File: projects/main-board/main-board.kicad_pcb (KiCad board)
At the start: 6 copper layers, 104.8 x 77 mm, 213 parts, among them J1 TC2030, J2 TC2030, J3 S3B-PH-SM4-TB, J4 USB4105-GF-A, J5 TC2030, J6 NHD-4.3-480272EF-ASXP (Molex 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, J7 USB4105-GF-A, J8 5051101292, J9 5051101292, Q1 ZXTN4240F-7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

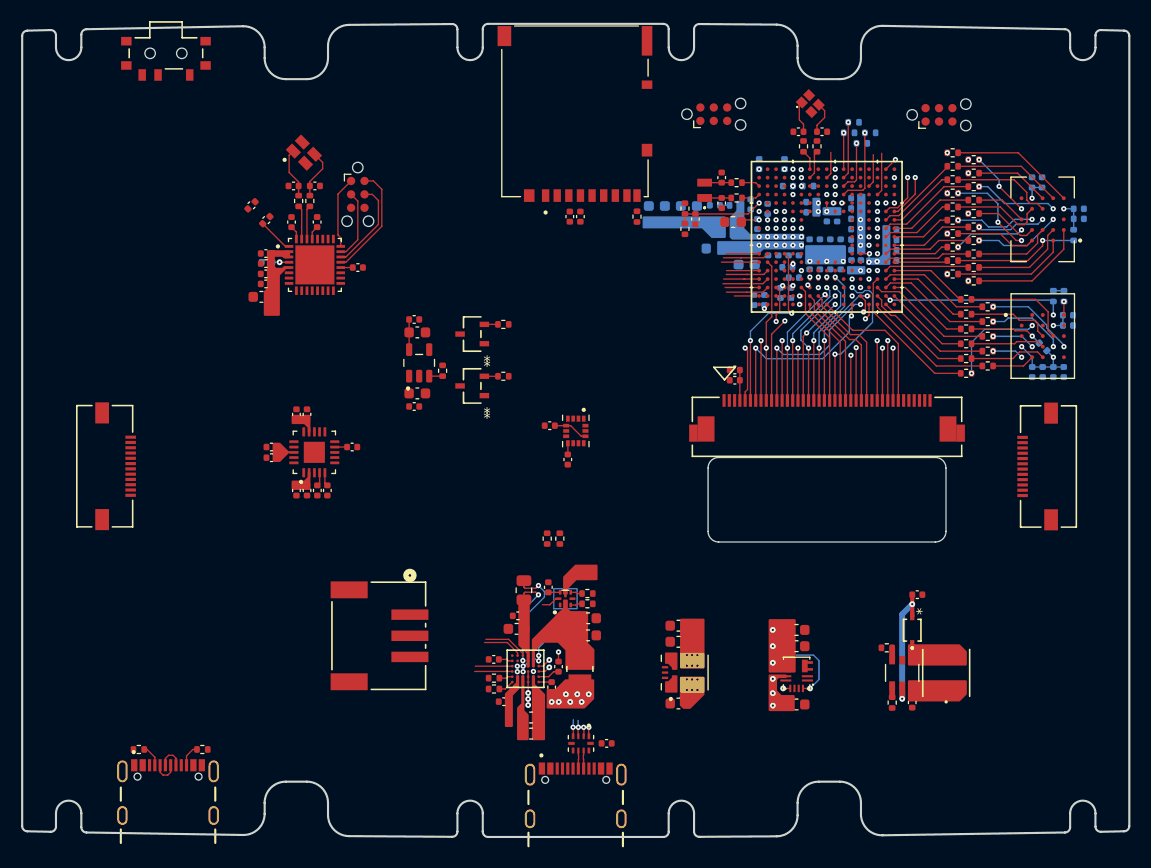
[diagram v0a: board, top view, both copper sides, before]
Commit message: Reorganise repo to support multiple PCBs
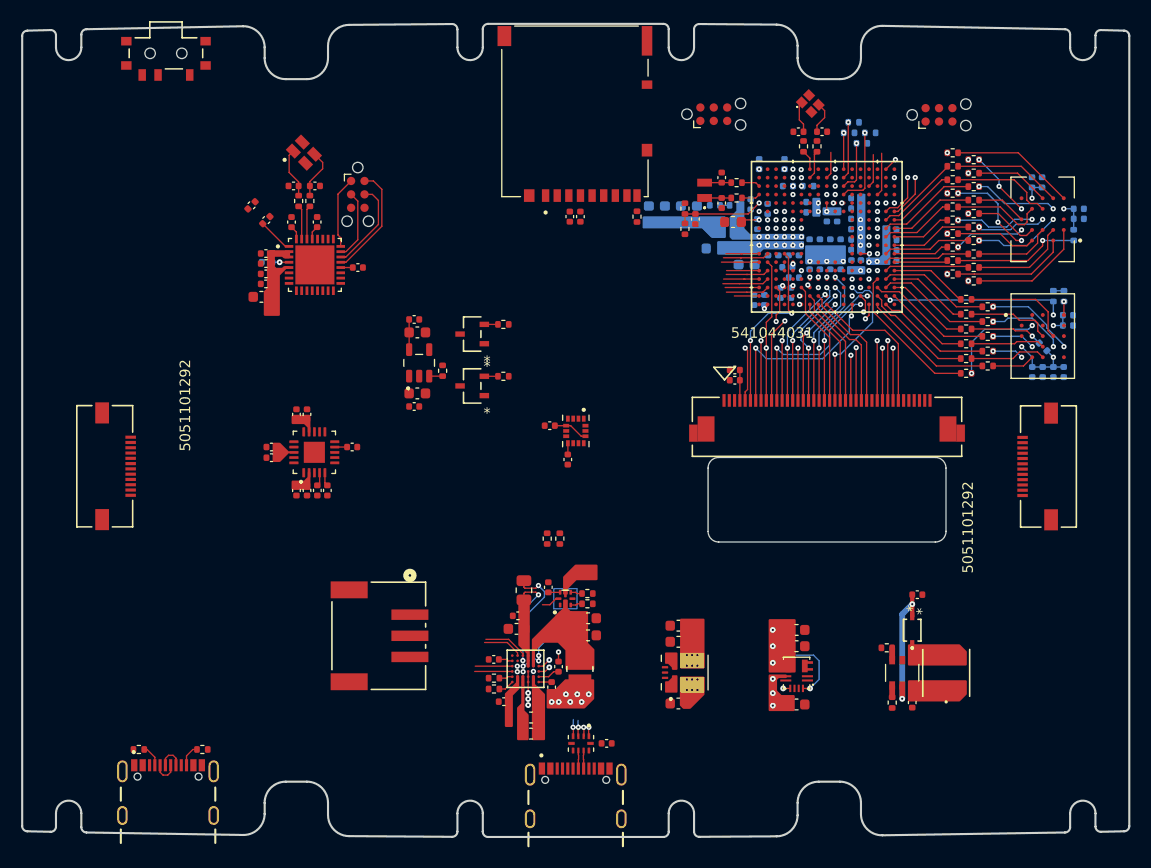
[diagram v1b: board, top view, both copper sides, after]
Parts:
- U4: value TPS22992RXPR -> TPS22992RXPR
- U7: value MAX77972EWX+T -> 21-100517_W363B3+1_ADI

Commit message: Fix wrong net name on left audio
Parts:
- U4: value TPS22992RXPR -> TPS22992RXPR
- U7: value 21-100517_W363B3+1_ADI -> MAX77972EWX+T
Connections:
- J8 pad 12: /Controllers/LEFT_MOTOR_N -> /Controllers/LEFT_MOTOR.N
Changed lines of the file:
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@@
 	(net 337 "/Audio/RIGHT_SPEAKER.N")
 	(net 338 "/Audio/LEFT_SPEAKER.N")
-	(net 339 "/Controllers/LEFT_MOTOR_N")
+	(net 339 "unconnected-(U5-NC-Pad3)")
 	(net 340 "/Controllers/RIGHT_MOTOR.P")
+	(net 341 "unconnected-(U6-NC-Pad2)")
+	(net 342 "unconnected-(U6-NC-Pad2)_2")
+	(net 343 "unconnected-(U6-NC-Pad2)_3")
+	(net 344 "unconnected-(U6-NC-Pad2)_4")
+	(net 345 "unconnected-(U6-NC-Pad2)_5")
+	(net 346 "unconnected-(U6-NC-Pad2)_6")
 	(footprint "Capacitor_SMD:C_0402_1005Metric"
 		(layer "F.Cu")
@@
 			(size 0.5 0.25)
 			(layers "F.Cu" "F.Mask" "F.Paste")
-			(net 287 "unconnected-(U5-NC-Pad3)_1")
+			(net 339 "unconnected-(U5-NC-Pad3)")
 			(pinfunction "NC")
 			(pintype "passive+no_connect")
@@
 			(layers "*.Cu")
 			(remove_unused_layers no)
-			(net 283 "unconnected-(U6-NC-Pad2)_1")
+			(net 343 "unconnected-(U6-NC-Pad2)_3")
 			(pinfunction "NC")
 			(pintype "passive+no_connect")
@@
 			(layers "*.Cu")
 			(remove_unused_layers no)
-			(net 283 "unconnected-(U6-NC-Pad2)_1")
+			(net 344 "unconnected-(U6-NC-Pad2)_4")
 			(pinfunction "NC")
 			(pintype "passive+no_connect")
@@
 			(size 0.5 0.5)
 			(layers "F.Cu")
-			(net 283 "unconnected-(U6-NC-Pad2)_1")
+			(net 341 "unconnected-(U6-NC-Pad2)")
 			(pinfunction "NC")
 			(pintype "passive+no_connect")
@@
 			(layers "*.Cu")
 			(remove_unused_layers no)
-			(net 283 "unconnected-(U6-NC-Pad2)_1")
+			(net 342 "unconnected-(U6-NC-Pad2)_2")
 			(pinfunction "NC")
 			(pintype "passive+no_connect")
@@
 			(layers "*.Cu")
 			(remove_unused_layers no)
-			(net 283 "unconnected-(U6-NC-Pad2)_1")
+			(net 345 "unconnected-(U6-NC-Pad2)_5")
 			(pinfunction "NC")
 			(pintype "passive+no_connect")
@@
 			(layers "*.Cu")
 			(remove_unused_layers no)
-			(net 283 "unconnected-(U6-NC-Pad2)_1")
+			(net 346 "unconnected-(U6-NC-Pad2)_6")
 			(pinfunction "NC")
 			(pintype "passive+no_connect")
@@
 			)
 		)
-		(property "Value" "21-100517_W363B3+1_ADI"
+		(property "Value" "MAX77972EWX+T"
 			(at 3.400001 -4.8 90)
 			(unlocked yes)
@@
 			(size 0.3 1)
 			(layers "F.Cu" "F.Mask" "F.Paste")
-			(net 339 "/Controllers/LEFT_MOTOR_N")
+			(net 319 "/Controllers/LEFT_MOTOR.N")
 			(pinfunction "Pin_12")
 			(pintype "passive")
@@
 			)
 		)
-		(property "Value" "TPS22992RXPR "
+		(property "Value" "TPS22992RXPR"
 			(at 3.8 1.9 90)
 			(layer "F.Fab")

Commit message: Position board-to-board connectors
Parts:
- moved J9 19.2 mm to (106.8, 121.6)
- moved J8 19.2 mm to (196.6, 121.6)
- moved C87 10.7 mm to (172.8, 124.5)
- moved R55 10.7 mm to (170.9, 124.5)
- moved C88 10.7 mm to (173.3, 114.3)
- moved D1 10.7 mm to (172.8, 117.6)
- moved L6 10.7 mm to (176.1, 121.7)
- moved R56 10.7 mm to (170.4, 119.3)
- moved U10 10.7 mm to (171.9, 121.7)
- moved C59 6.79 mm to (165.8, 124.7)
- moved C62 6.79 mm to (165.8, 119.2)
- moved U5 6.79 mm to (165.8, 121.7)
- moved C61 6.79 mm to (165.8, 117.6)
- moved U6 2.96 mm to (159.1, 121.8)
- moved C63 2.96 mm to (158.5, 124.7)
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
